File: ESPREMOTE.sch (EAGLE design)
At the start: 38 parts, among them IC1 ESP12SMT, IC3 LD111733, P1 USB-6PSMT, Q1 2N7002, Q2 2N7002, Q3 2N7002, Q4 2N7002

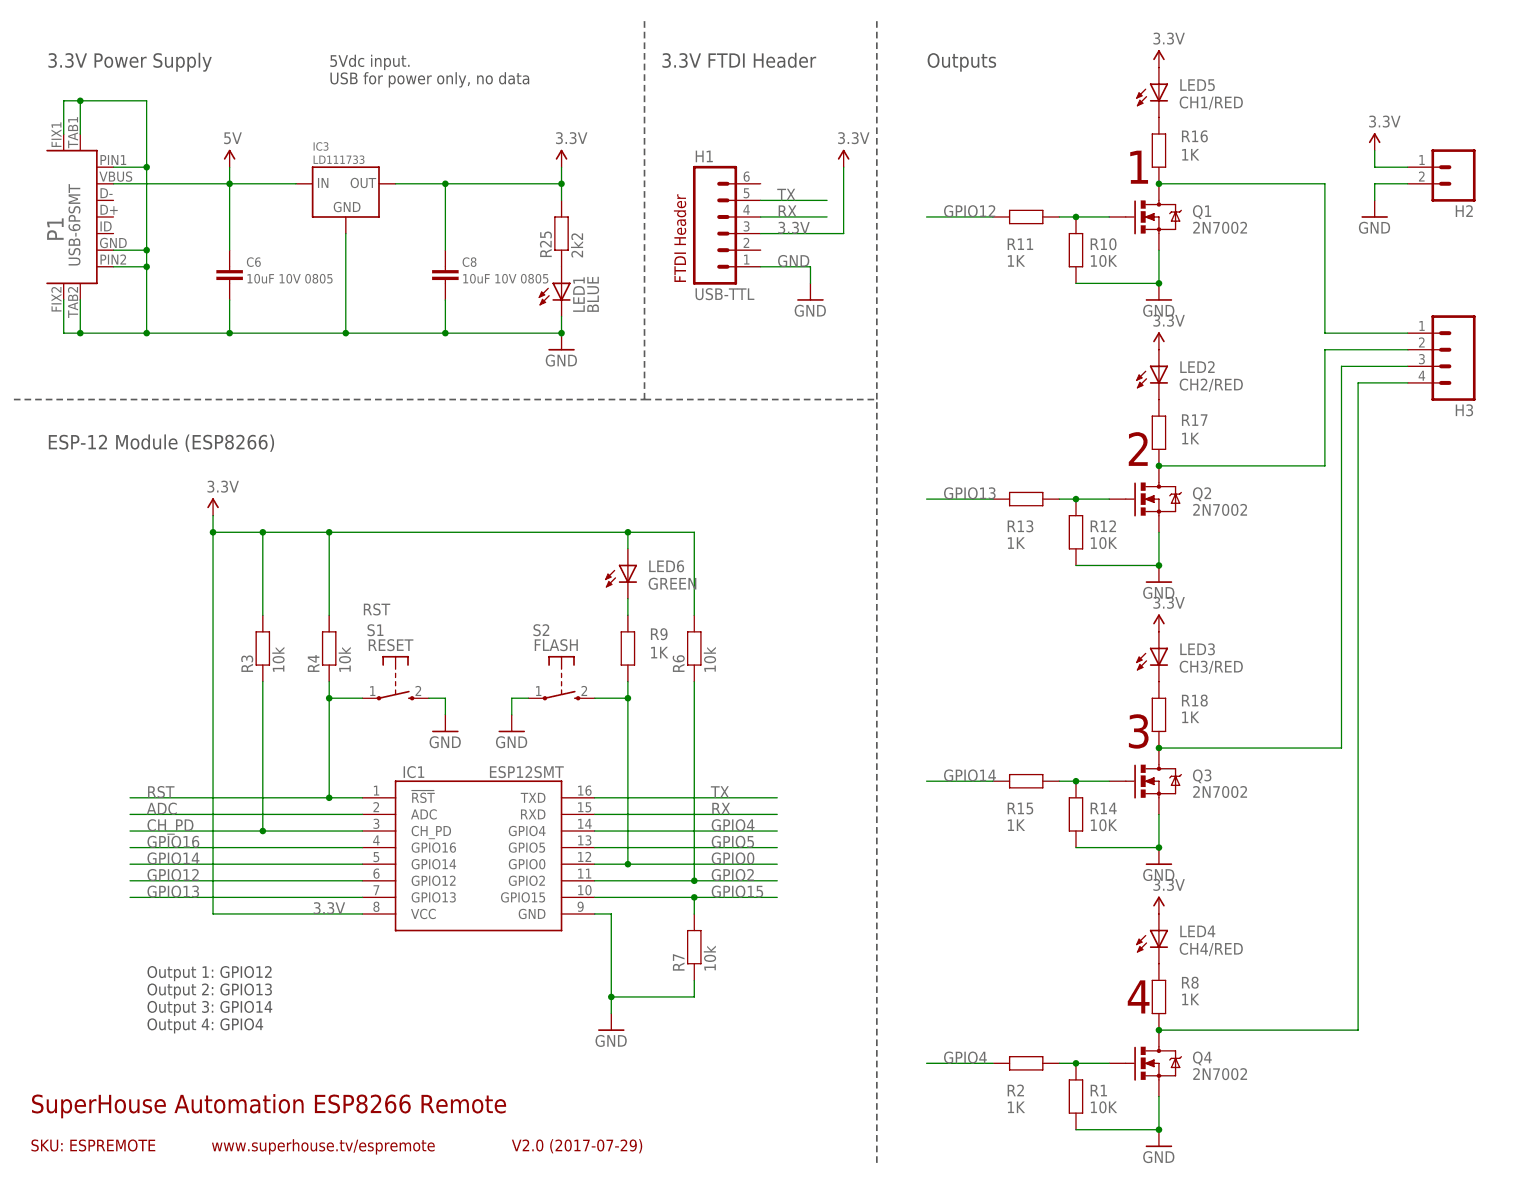
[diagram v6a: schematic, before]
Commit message: Replaced USB socket and linear reg with 2.1mm DC jack and SMPS module
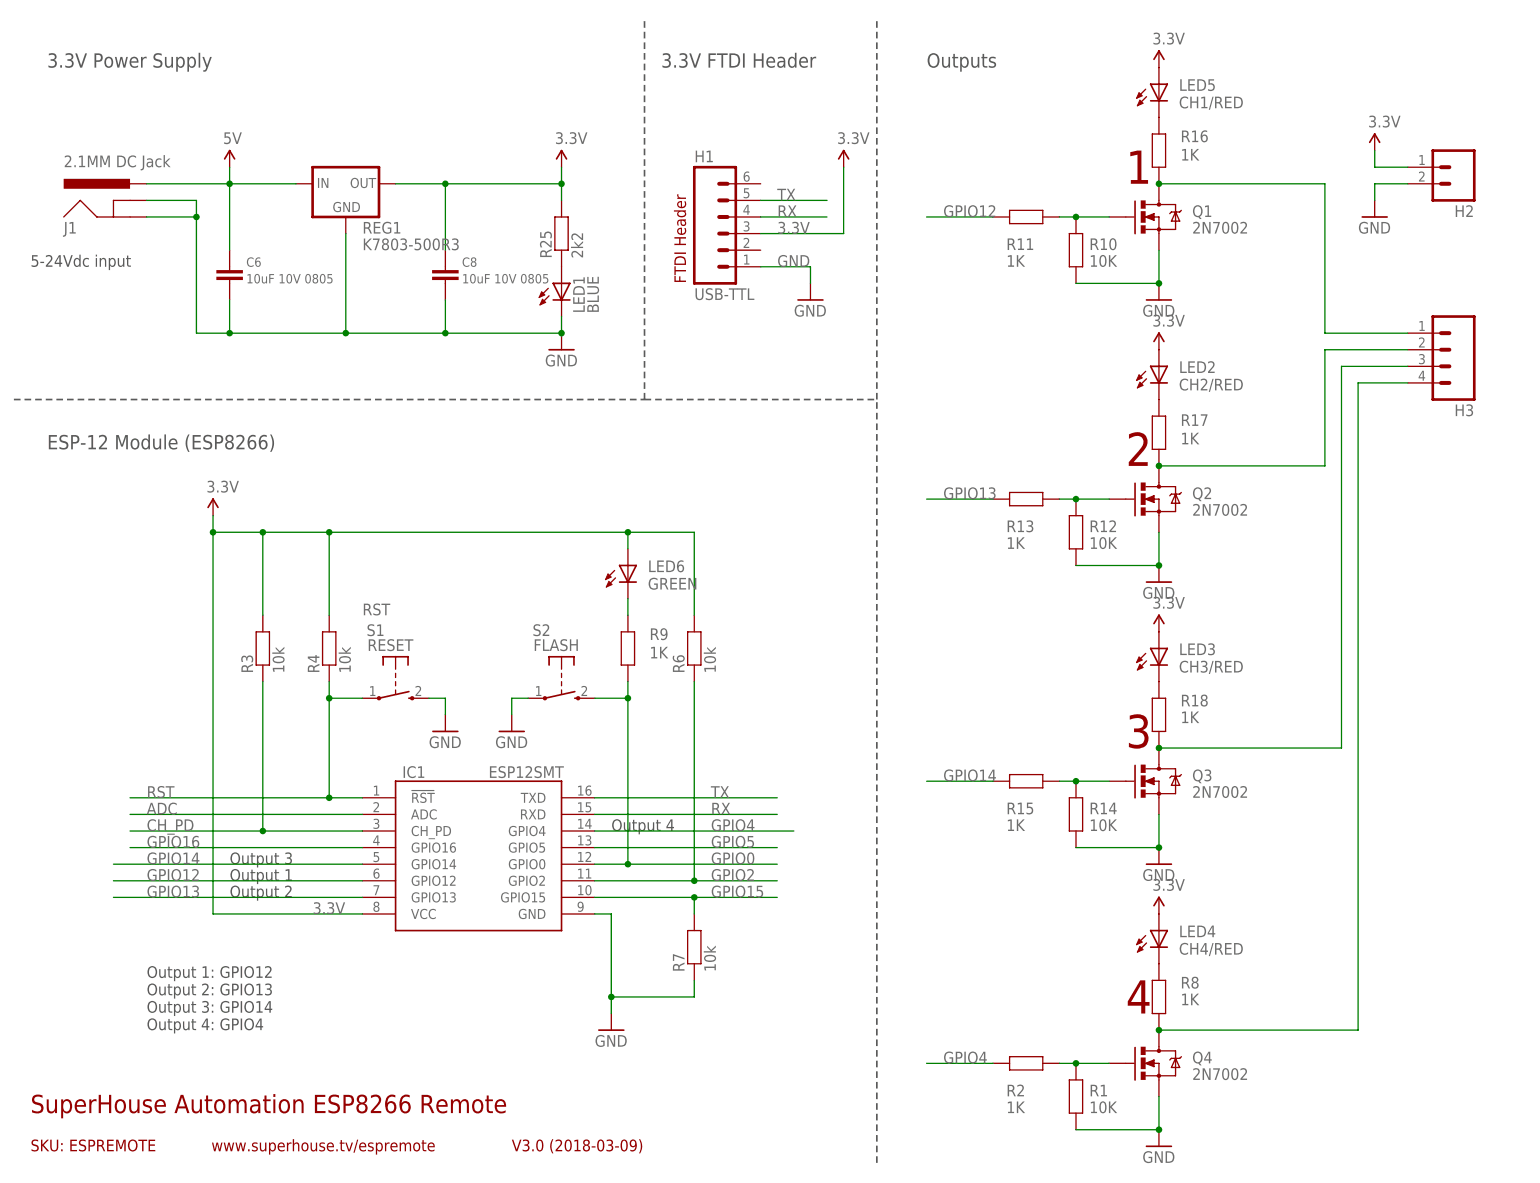
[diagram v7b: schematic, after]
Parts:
- removed IC3: LD111733, freetronics-luke:LD1117-FIXED
- removed P1: USB-6PSMT, freetronics-jon:USB-6PSMT
- added J1: 2.1MM DC Jack, freetronics-jon:POWER_JACKPTH_SLOTS
- added REG1: K7803-500R3, freetronics-jon:K78XX-500R3
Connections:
- net 3.3V: now also REG1.OUT; no longer IC3.OUT
- net 5V: now also J1.PWR, REG1.IN; no longer IC3.IN, P1.VBUS
- net GND: now also J1.GND, J1.GNDBREAK, REG1.GND; no longer IC3.GND, P1.FIX1, P1.FIX2, P1.GND, P1.PIN1, P1.PIN2, P1.TAB1, P1.TAB2
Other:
- note added: "5-24Vdc input"
- note added: "Output 1"
- note added: "Output 2"
- note added: "Output 3"
- note added: "Output 4"
- note added: "V3.0 (2018-03-09)"
- note removed: "5Vdc input. USB for power only, no data"
- note removed: "SOT-223"
- note removed: "V2.0 (2017-07-29)"
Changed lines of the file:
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@@
 <?xml version="1.0" encoding="utf-8"?>
 <!DOCTYPE eagle SYSTEM "eagle.dtd">
-<eagle version="8.4.2">
+<eagle version="8.6.0">
 <drawing>
 <settings>
@@
 <layer number="60" name="bCarbon" color="7" fill="1" visible="no" active="no"/>
 <layer number="61" name="pt_docu" color="7" fill="0" visible="no" active="no"/>
+<layer number="88" name="SimResults" color="9" fill="1" visible="yes" active="yes"/>
+<layer number="89" name="SimProbes" color="9" fill="1" visible="yes" active="yes"/>
 <layer number="90" name="Modules" color="5" fill="1" visible="yes" active="yes"/>
 <layer number="91" name="Nets" color="2" fill="1" visible="yes" active="yes"/>
@@
 <part name="R9" library="freetronics-master-v1" deviceset="RESISTOR" device="0603" value="1K"/>
 <part name="C6" library="freetronics-jon" deviceset="C-EU" device="C0805" value="10uF 10V 0805"/>
-<part name="IC3" library="freetronics-luke" deviceset="LD1117-FIXED" device="" value="LD111733"/>
 <part name="U$4" library="freetronics-original" deviceset="5V" device=""/>
-<part name="P1" library="freetronics-jon" deviceset="USB-6P" device="SMT"/>
 <part name="GND7" library="SparkFun" deviceset="GND" device=""/>
+<part name="REG1" library="freetronics-jon" deviceset="K78XX-500R3" device="" value="K7803-500R3"/>
+<part name="J1" library="freetronics-jon" deviceset="POWER_JACK" device="PTH_SLOTS" value="2.1MM DC Jack"/>
 </parts>
 <sheets>
@@
 <text x="7.62" y="6.858" size="1.778" layer="94">SKU: ESPREMOTE</text>
 <text x="7.62" y="12.7" size="2.794" layer="94">SuperHouse Automation ESP8266 Remote</text>
-<text x="81.28" y="6.858" size="1.778" layer="94">V2.0 (2017-07-29)</text>
+<text x="81.28" y="6.858" size="1.778" layer="94">V3.0 (2018-03-09)</text>
 <text x="35.306" y="6.858" size="1.778" layer="94">www.superhouse.tv/espremote</text>
 <frame x1="5.08" y1="5.08" x2="109.22" y2="17.78" columns="0" rows="0" layer="94" border-left="no" border-top="no" border-right="no" border-bottom="no"/>
@@
 <text x="10.16" y="114.3" size="2.1844" layer="97" font="vector" ratio="15">ESP-12 Module (ESP8266)</text>
 <text x="104.14" y="172.72" size="2.1844" layer="97" font="vector" ratio="15">3.3V FTDI Header</text>
-<text x="53.34" y="170.18" size="1.778" layer="97" font="vector" ratio="10">5Vdc input.
-USB for power only, no data</text>
+<text x="7.62" y="142.24" size="1.778" layer="97" font="vector" ratio="10">5-24Vdc input</text>
 <text x="25.4" y="25.4" size="1.778" layer="97" font="vector" ratio="10">Output 1: GPIO12
 Output 2: GPIO13
 Output 3: GPIO14
 Output 4: GPIO4</text>
-<text x="50.8" y="162.56" size="1.27" layer="98">SOT-223</text>
+<text x="38.1" y="48.26" size="1.778" layer="97">Output 1</text>
+<text x="38.1" y="45.72" size="1.778" layer="97">Output 2</text>
+<text x="38.1" y="50.8" size="1.778" layer="97">Output 3</text>
+<text x="96.52" y="55.88" size="1.778" layer="97">Output 4</text>
 </plain>
 <instances>
@@
 <attribute name="VALUE" x="40.64" y="139.7" size="1.4224" layer="96"/>
 </instance>
-<instance part="IC3" gate="G$1" x="55.88" y="152.4" smashed="yes">
-<attribute name="NAME" x="50.8" y="160.02" size="1.27" layer="95"/>
-<attribute name="VALUE" x="50.8" y="157.988" size="1.27" layer="96"/>
-</instance>
 <instance part="U$4" gate="G$1" x="38.1" y="157.48"/>
-<instance part="P1" gate="G$1" x="15.24" y="149.86" smashed="yes" rot="R180">
-<attribute name="NAME" x="12.7" y="146.05" size="2.54" layer="95" rot="R90"/>
-<attribute name="VALUE" x="15.24" y="142.24" size="1.778" layer="96" rot="R90"/>
-</instance>
 <instance part="GND7" gate="1" x="88.9" y="129.54"/>
+<instance part="REG1" gate="G$1" x="55.88" y="154.94"/>
+<instance part="J1" gate="G$1" x="22.86" y="147.32"/>
 </instances>
 <busses>
@@
 <wire x1="38.1" y1="132.08" x2="55.88" y2="132.08" width="0.1524" layer="91"/>
 <wire x1="55.88" y1="132.08" x2="55.88" y2="147.32" width="0.1524" layer="91"/>
-<pinref part="IC3" gate="G$1" pin="GND"/>
 <junction x="55.88" y="132.08"/>
 <wire x1="55.88" y1="132.08" x2="71.12" y2="132.08" width="0.1524" layer="91"/>
 <wire x1="38.1" y1="137.16" x2="38.1" y2="132.08" width="0.1524" layer="91"/>
 <junction x="38.1" y="132.08"/>
-<pinref part="P1" gate="G$1" pin="GND"/>
-<wire x1="20.32" y1="144.78" x2="25.4" y2="144.78" width="0.1524" layer="91"/>
-<wire x1="25.4" y1="144.78" x2="25.4" y2="142.24" width="0.1524" layer="91"/>
-<pinref part="P1" gate="G$1" pin="PIN2"/>
-<wire x1="20.32" y1="142.24" x2="25.4" y2="142.24" width="0.1524" layer="91"/>
-<pinref part="P1" gate="G$1" pin="PIN1"/>
-<wire x1="20.32" y1="157.48" x2="25.4" y2="157.48" width="0.1524" layer="91"/>
-<wire x1="25.4" y1="157.48" x2="25.4" y2="144.78" width="0.1524" layer="91"/>
-<wire x1="25.4" y1="142.24" x2="25.4" y2="132.08" width="0.1524" layer="91"/>
-<wire x1="25.4" y1="132.08" x2="15.24" y2="132.08" width="0.1524" layer="91"/>
-<pinref part="P1" gate="G$1" pin="TAB2"/>
-<wire x1="15.24" y1="132.08" x2="15.24" y2="137.16" width="0.1524" layer="91"/>
-<wire x1="15.24" y1="132.08" x2="12.7" y2="132.08" width="0.1524" layer="91"/>
-<pinref part="P1" gate="G$1" pin="FIX2"/>
-<wire x1="12.7" y1="132.08" x2="12.7" y2="137.16" width="0.1524" layer="91"/>
-<wire x1="25.4" y1="157.48" x2="25.4" y2="167.64" width="0.1524" layer="91"/>
-<pinref part="P1" gate="G$1" pin="TAB1"/>
-<wire x1="25.4" y1="167.64" x2="15.24" y2="167.64" width="0.1524" layer="91"/>
-<wire x1="15.24" y1="167.64" x2="15.24" y2="162.56" width="0.1524" layer="91"/>
-<pinref part="P1" gate="G$1" pin="FIX1"/>
-<wire x1="15.24" y1="167.64" x2="12.7" y2="167.64" width="0.1524" layer="91"/>
-<wire x1="12.7" y1="167.64" x2="12.7" y2="162.56" width="0.1524" layer="91"/>
-<junction x="15.24" y="132.08"/>
-<junction x="25.4" y="142.24"/>
-<junction x="25.4" y="144.78"/>
-<junction x="25.4" y="157.48"/>
-<junction x="15.24" y="167.64"/>
-<wire x1="25.4" y1="132.08" x2="38.1" y2="132.08" width="0.1524" layer="91"/>
+<wire x1="33.02" y1="132.08" x2="38.1" y2="132.08" width="0.1524" layer="91"/>
 <pinref part="GND7" gate="1" pin="GND"/>
 <junction x="88.9" y="132.08"/>
-<junction x="25.4" y="132.08"/>
+<pinref part="REG1" gate="G$1" pin="GND"/>
+<pinref part="J1" gate="G$1" pin="GNDBREAK"/>
+<wire x1="25.4" y1="152.4" x2="33.02" y2="152.4" width="0.1524" layer="91"/>
+<wire x1="33.02" y1="152.4" x2="33.02" y2="149.86" width="0.1524" layer="91"/>
+<pinref part="J1" gate="G$1" pin="GND"/>
+<wire x1="33.02" y1="149.86" x2="33.02" y2="132.08" width="0.1524" layer="91"/>
+<wire x1="25.4" y1="149.86" x2="33.02" y2="149.86" width="0.1524" layer="91"/>
+<junction x="33.02" y="149.86"/>
 </segment>
 <segment>
@@
 <segment>
 <pinref part="IC1" gate="G$1" pin="GPIO4"/>
-<wire x1="93.98" y1="55.88" x2="121.92" y2="55.88" width="0.1524" layer="91"/>
+<wire x1="93.98" y1="55.88" x2="124.46" y2="55.88" width="0.1524" layer="91"/>
 <label x="111.76" y="55.88" size="1.778" layer="95"/>
 </segment>
@@
 <segment>
 <pinref part="IC1" gate="G$1" pin="GPIO14"/>
-<wire x1="58.42" y1="50.8" x2="22.86" y2="50.8" width="0.1524" layer="91"/>
+<wire x1="58.42" y1="50.8" x2="20.32" y2="50.8" width="0.1524" layer="91"/>
 <label x="25.4" y="50.8" size="1.778" layer="95"/>
 </segment>
@@
 <segment>
 <pinref part="IC1" gate="G$1" pin="GPIO12"/>
-<wire x1="58.42" y1="48.26" x2="22.86" y2="48.26" width="0.1524" layer="91"/>
+<wire x1="58.42" y1="48.26" x2="20.32" y2="48.26" width="0.1524" layer="91"/>
 <label x="25.4" y="48.26" size="1.778" layer="95"/>
 </segment>
@@
 <segment>
 <pinref part="IC1" gate="G$1" pin="GPIO13"/>
-<wire x1="58.42" y1="45.72" x2="22.86" y2="45.72" width="0.1524" layer="91"/>
+<wire x1="58.42" y1="45.72" x2="20.32" y2="45.72" width="0.1524" layer="91"/>
 <label x="25.4" y="45.72" size="1.778" layer="95"/>
 </segment>
@@
 </segment>
 <segment>
-<pinref part="IC3" gate="G$1" pin="OUT"/>
 <pinref part="R25" gate="G$1" pin="2"/>
 <wire x1="88.9" y1="157.48" x2="88.9" y2="154.94" width="0.1524" layer="91"/>
@@
 <wire x1="88.9" y1="154.94" x2="71.12" y2="154.94" width="0.1524" layer="91"/>
 <junction x="88.9" y="154.94"/>
+<pinref part="REG1" gate="G$1" pin="OUT"/>
 </segment>
 </net>
@@
 <net name="5V" class="0">
 <segment>
-<wire x1="20.32" y1="154.94" x2="38.1" y2="154.94" width="0.1524" layer="91"/>
 <wire x1="38.1" y1="154.94" x2="48.26" y2="154.94" width="0.1524" layer="91"/>
 <pinref part="C6" gate="G$1" pin="1"/>
 <wire x1="38.1" y1="144.78" x2="38.1" y2="154.94" width="0.1524" layer="91"/>
 <junction x="38.1" y="154.94"/>
-<pinref part="IC3" gate="G$1" pin="IN"/>
 <wire x1="38.1" y1="154.94" x2="38.1" y2="157.48" width="0.1524" layer="91"/>
 <pinref part="U$4" gate="G$1" pin="5V"/>
-<pinref part="P1" gate="G$1" pin="VBUS"/>
-</segment>
-</net>
+<pinref part="REG1" gate="G$1" pin="IN"/>
+<pinref part="J1" gate="G$1" pin="PWR"/>
+<wire x1="38.1" y1="154.94" x2="25.4" y2="154.94" width="0.1524" layer="91"/>
+</segment>
+</net>

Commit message: Improved labels for v3.0 release
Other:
- note added: "Tx Buttons"
- note added: "Tx Power"
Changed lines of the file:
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@@
 <text x="38.1" y="50.8" size="1.778" layer="97">Output 3</text>
 <text x="96.52" y="55.88" size="1.778" layer="97">Output 4</text>
+<text x="220.98" y="162.56" size="1.778" layer="97">Tx Power</text>
+<text x="220.98" y="137.16" size="1.778" layer="97">Tx Buttons</text>
 </plain>
 <instances>
